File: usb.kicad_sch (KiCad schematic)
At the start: 0 parts

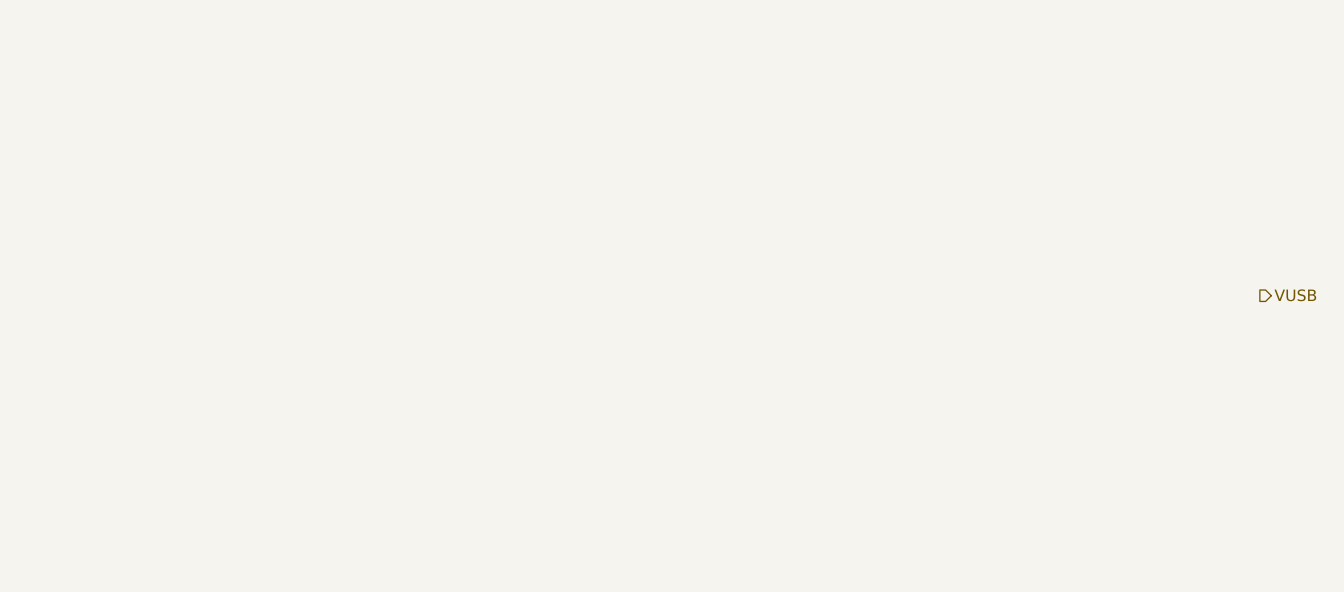
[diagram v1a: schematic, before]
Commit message: Finish rough layout
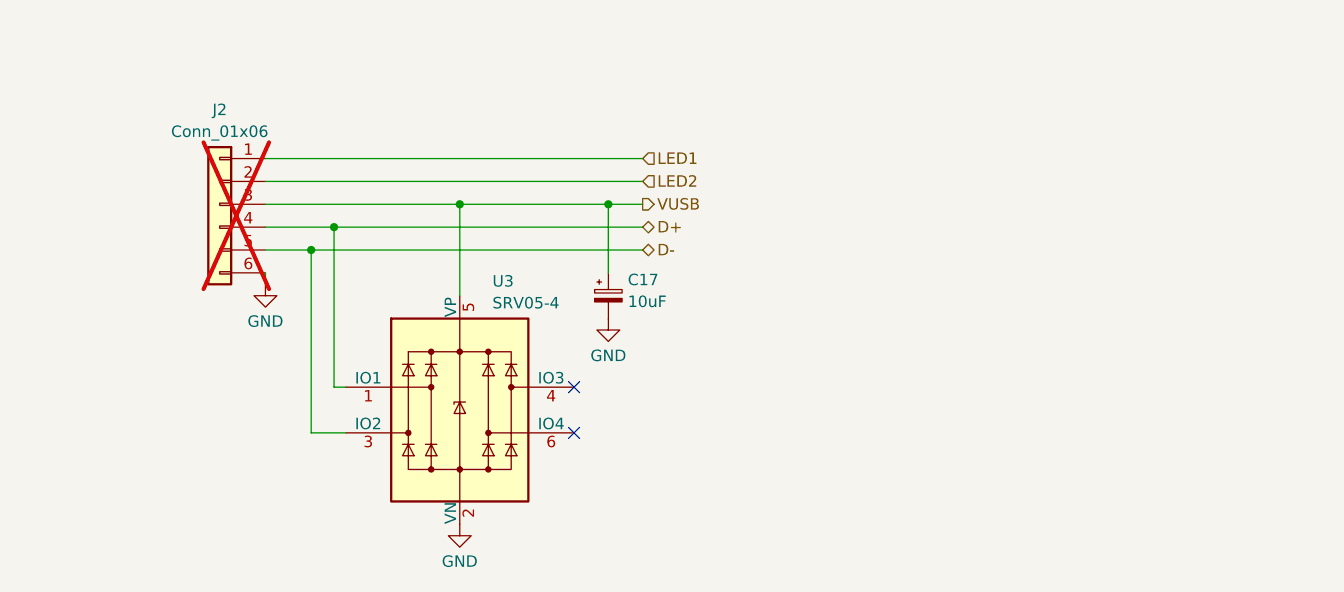
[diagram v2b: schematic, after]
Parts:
- added C17: 10uF, Capacitor_Tantalum_SMD:CP_EIA-3216-18_Kemet-A, symbol Device:C_Polarized_Small
- added J2: Conn_01x06, Connector_PinHeader_2.00mm:PinHeader_1x06_P2.00mm_Vertical, symbol Connector_Generic:Conn_01x06
- added U3: SRV05-4, Package_TO_SOT_SMD:SOT-23-6, symbol Power_Protection:SRV05-4
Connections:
- net VUSB: now also C17.1, J2.3 (Pin_3), U3.5 (VP)
- new net D+: J2.4 (Pin_4), U3.1 (IO1)
- new net D-: J2.5 (Pin_5), U3.3 (IO2)
- new net GND: C17.2, J2.6 (Pin_6), U3.2 (VN)
- new net LED1: J2.1 (Pin_1)
- new net LED2: J2.2 (Pin_2)
- no-connect marks 0 -> 2
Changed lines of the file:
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@@
 (kicad_sch (version 20230121) (generator eeschema)
   (paper "A4")
-  (hierarchical_label "VUSB" (shape output) (at 233.68 82.55 0) (fields_autoplaced)
-    (effects (font (size 1.27 1.27)) (justify left))
+  (junction (at 144.78 72.39) (diameter 0) (color 0 0 0 0)
+  )
+  (junction (at 130.81 74.93) (diameter 0) (color 0 0 0 0)
+  )
+  (junction (at 128.27 77.47) (diameter 0) (color 0 0 0 0)
+  )
+  (junction (at 161.29 72.39) (diameter 0) (color 0 0 0 0)
+  )
+  (no_connect (at 157.48 92.71))
+  (no_connect (at 157.48 97.79))
+  (wire (pts (xy 123.19 72.39) (xy 144.78 72.39))
+    (stroke (width 0) (type default))
+  )
+  (wire (pts (xy 123.19 80.01) (xy 123.19 81.28))
+    (stroke (width 0) (type default))
+  )
+  (wire (pts (xy 132.08 92.71) (xy 130.81 92.71))
+    (stroke (width 0) (type default))
+  )
+  (wire (pts (xy 130.81 74.93) (xy 165.1 74.93))
+    (stroke (width 0) (type default))
+  )
+  (wire (pts (xy 144.78 72.39) (xy 144.78 82.55))
+    (stroke (width 0) (type default))
+  )
+  (wire (pts (xy 128.27 97.79) (xy 128.27 77.47))
+    (stroke (width 0) (type default))
+  )
+  (wire (pts (xy 165.1 72.39) (xy 161.29 72.39))
+    (stroke (width 0) (type default))
+  )
+  (wire (pts (xy 123.19 74.93) (xy 130.81 74.93))
+    (stroke (width 0) (type default))
+  )
+  (wire (pts (xy 123.19 67.31) (xy 165.1 67.31))
+    (stroke (width 0) (type default))
+  )
+  (wire (pts (xy 161.29 72.39) (xy 161.29 80.01))
+    (stroke (width 0) (type default))
+  )
+  (wire (pts (xy 144.78 72.39) (xy 161.29 72.39))
+    (stroke (width 0) (type default))
+  )
+  (wire (pts (xy 123.19 77.47) (xy 128.27 77.47))
+    (stroke (width 0) (type default))
+  )
+  (wire (pts (xy 130.81 74.93) (xy 130.81 92.71))
+    (stroke (width 0) (type default))
+  )
+  (wire (pts (xy 123.19 69.85) (xy 165.1 69.85))
+    (stroke (width 0) (type default))
+  )
+  (wire (pts (xy 128.27 77.47) (xy 165.1 77.47))
+    (stroke (width 0) (type default))
+  )
+  (wire (pts (xy 132.08 97.79) (xy 128.27 97.79))
+    (stroke (width 0) (type default))
+  )
+  (hierarchical_label "LED1" (shape input) (at 165.1 67.31 0) (fields_autoplaced)
+    (effects (font (size 1.27 1.27)) (justify left))
+  )
+  (hierarchical_label "LED2" (shape input) (at 165.1 69.85 0) (fields_autoplaced)
+    (effects (font (size 1.27 1.27)) (justify left))
+  )
+  (hierarchical_label "D-" (shape bidirectional) (at 165.1 77.47 0) (fields_autoplaced)
+    (effects (font (size 1.27 1.27)) (justify left))
+  )
+  (hierarchical_label "D+" (shape bidirectional) (at 165.1 74.93 0) (fields_autoplaced)
+    (effects (font (size 1.27 1.27)) (justify left))
+  )
+  (hierarchical_label "VUSB" (shape output) (at 165.1 72.39 0) (fields_autoplaced)
+    (effects (font (size 1.27 1.27)) (justify left))
+  )
+  (symbol (lib_id "power:GND") (at 161.29 85.09 0) (unit 1)
+    (in_bom yes) (on_board yes) (dnp no) (fields_autoplaced)
+    (property "Reference" "#PWR036" (at 161.29 91.44 0)
+      (effects (font (size 1.27 1.27)) hide)
+    )
+    (property "Value" "GND" (at 161.29 89.2231 0)
+      (effects (font (size 1.27 1.27)))
+    )
+    (property "Footprint" "" (at 161.29 85.09 0)
+      (effects (font (size 1.27 1.27)) hide)
+    )
+    (property "Datasheet" "" (at 161.29 85.09 0)
+      (effects (font (size 1.27 1.27)) hide)
+    )
+    (pin "1")
+    (instances
+      (project "blinkekatze"
+        (path "/20b2a5b0-0a80-4b97-84d4-d5290b2926e5/8601bd41-9983-455b-8dd5-e9b320509b2a"
+          (reference "#PWR036") (unit 1)
+        )
+      )
+    )
+  )
+  (symbol (lib_id "Device:C_Polarized_Small") (at 161.29 82.55 0) (unit 1)
+    (in_bom yes) (on_board yes) (dnp no) (fields_autoplaced)
+    (property "Reference" "C17" (at 163.449 80.7918 0)
+      (effects (font (size 1.27 1.27)) (justify left))
+    )
+    (property "Value" "10uF" (at 163.449 83.216 0)
+      (effects (font (size 1.27 1.27)) (justify left))
+    )
+    (property "Footprint" "Capacitor_Tantalum_SMD:CP_EIA-3216-18_Kemet-A" (at 161.29 82.55 0)
+      (effects (font (size 1.27 1.27)) hide)
+    )
+    (property "Datasheet" "~" (at 161.29 82.55 0)
+      (effects (font (size 1.27 1.27)) hide)
+    )
+    (property "LCSC" "C7171" (at 161.29 82.55 0)
+      (effects (font (size 1.27 1.27)) hide)
+    )
+    (pin "1")
+    (pin "2")
+    (instances
+      (project "blinkekatze"
+        (path "/20b2a5b0-0a80-4b97-84d4-d5290b2926e5/8601bd41-9983-455b-8dd5-e9b320509b2a"
+          (reference "C17") (unit 1)
+        )
+      )
+    )
+  )
+  (symbol (lib_id "power:GND") (at 123.19 81.28 0) (unit 1)
+    (in_bom yes) (on_board yes) (dnp no) (fields_autoplaced)
+    (property "Reference" "#PWR035" (at 123.19 87.63 0)
+      (effects (font (size 1.27 1.27)) hide)
+    )
+    (property "Value" "GND" (at 123.19 85.4131 0)
+      (effects (font (size 1.27 1.27)))
+    )
+    (property "Footprint" "" (at 123.19 81.28 0)
+      (effects (font (size 1.27 1.27)) hide)
+    )
+    (property "Datasheet" "" (at 123.19 81.28 0)
+      (effects (font (size 1.27 1.27)) hide)
+    )
+    (pin "1")
+    (instances
+      (project "blinkekatze"
+        (path "/20b2a5b0-0a80-4b97-84d4-d5290b2926e5/8601bd41-9983-455b-8dd5-e9b320509b2a"
+          (reference "#PWR035") (unit 1)
+        )
+      )
+    )
+  )
+  (symbol (lib_id "Power_Protection:SRV05-4") (at 144.78 95.25 0) (unit 1)
+    (in_bom yes) (on_board yes) (dnp no) (fields_autoplaced)
+    (property "Reference" "U3" (at 148.4061 80.9457 0)
+      (effects (font (size 1.27 1.27)) (justify left))
+    )
+    (property "Value" "SRV05-4" (at 148.4061 83.3699 0)
+      (effects (font (size 1.27 1.27)) (justify left))
+    )
+    (property "Footprint" "Package_TO_SOT_SMD:SOT-23-6" (at 162.56 106.68 0)
+      (effects (font (size 1.27 1.27)) hide)
+    )
+    (property "Datasheet" "http://www.onsemi.com/pub/Collateral/SRV05-4-D.PDF" (at 144.78 95.25 0)
+      (effects (font (size 1.27 1.27)) hide)
+    )
+    (property "LCSC" "C85364" (at 144.78 95.25 0)
+      (effects (font (size 1.27 1.27)) hide)
+    )
+    (pin "1")
+    (pin "2")
+    (pin "3")
+    (pin "4")
+    (pin "5")
+    (pin "6")
+    (instances
+      (project "blinkekatze"
+        (path "/20b2a5b0-0a80-4b97-84d4-d5290b2926e5/8601bd41-9983-455b-8dd5-e9b320509b2a"
+          (reference "U3") (unit 1)
+        )
+      )
+    )
+  )
+  (symbol (lib_id "power:GND") (at 144.78 107.95 0) (unit 1)
+    (in_bom yes) (on_board yes) (dnp no) (fields_autoplaced)
+    (property "Reference" "#PWR037" (at 144.78 114.3 0)
+      (effects (font (size 1.27 1.27)) hide)
+    )
+    (property "Value" "GND" (at 144.78 112.0831 0)
+      (effects (font (size 1.27 1.27)))
+    )
+    (property "Footprint" "" (at 144.78 107.95 0)
+      (effects (font (size 1.27 1.27)) hide)
+    )
+    (property "Datasheet" "" (at 144.78 107.95 0)
+      (effects (font (size 1.27 1.27)) hide)
+    )
+    (pin "1")
+    (instances
+      (project "blinkekatze"
+        (path "/20b2a5b0-0a80-4b97-84d4-d5290b2926e5/8601bd41-9983-455b-8dd5-e9b320509b2a"
+          (reference "#PWR037") (unit 1)
+        )
+      )
+    )
+  )
+  (symbol (lib_id "Connector_Generic:Conn_01x06") (at 118.11 72.39 0) (mirror y) (unit 1)
+    (in_bom no) (on_board yes) (dnp yes) (fields_autoplaced)
+    (property "Reference" "J2" (at 118.11 61.8957 0)
+      (effects (font (size 1.27 1.27)))
+    )
+    (property "Value" "Conn_01x06" (at 118.11 64.3199 0)
+      (effects (font (size 1.27 1.27)))
+    )
+    (property "Footprint" "Connector_PinHeader_2.00mm:PinHeader_1x06_P2.00mm_Vertical" (at 118.11 72.39 0)
+      (effects (font (size 1.27 1.27)) hide)
+    )
+    (property "Datasheet" "~" (at 118.11 72.39 0)
+      (effects (font (size 1.27 1.27)) hide)
+    )
+    (pin "1")
+    (pin "2")
+    (pin "3")
+    (pin "4")
+    (pin "5")
+    (pin "6")
+    (instances
+      (project "blinkekatze"
+        (path "/20b2a5b0-0a80-4b97-84d4-d5290b2926e5/8601bd41-9983-455b-8dd5-e9b320509b2a"
+          (reference "J2") (unit 1)
+        )
+      )
+    )
   )
 )

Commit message: Relayout board to fit constraints of Micro USB Blinkekatzen
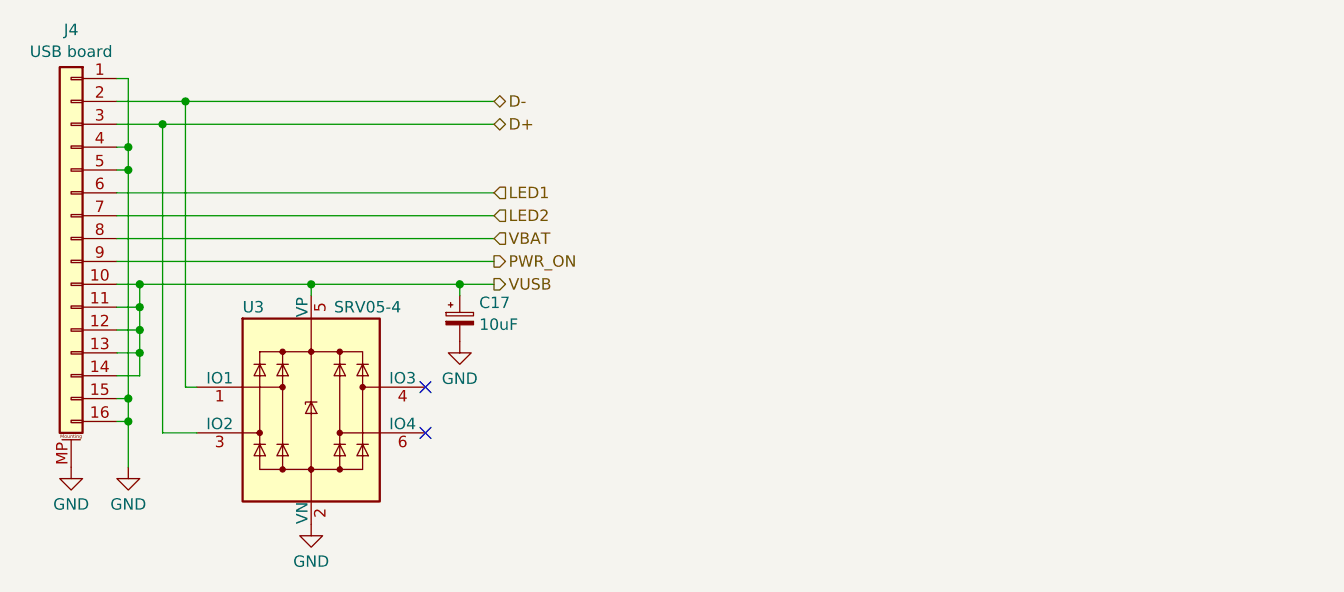
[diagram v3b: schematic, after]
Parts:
- removed J2: Conn_01x06, Connector_PinHeader_2.00mm:PinHeader_1x06_P2.00mm_Vertical, symbol Connector_Generic:Conn_01x06
- added J4: USB board, Connector_FFC-FPC_HDGC:0.5K-QX-16PWB_16Pin_0.5mm, symbol Connector_Generic_MountingPin:Conn_01x16_MountingPin
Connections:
- net D+: now also U3.3 (IO2), J4.3 (Pin_3); no longer U3.1 (IO1)
- net D-: now also U3.1 (IO1), J4.2 (Pin_2); no longer U3.3 (IO2)
- net GND: now also J4.1 (Pin_1), J4.15 (Pin_15), J4.16 (Pin_16), J4.4 (Pin_4), J4.5 (Pin_5), J4.MP (MountPin)
- net LED1: now also J4.6 (Pin_6)
- net LED2: now also J4.7 (Pin_7)
- net VUSB: now also J4.10 (Pin_10), J4.11 (Pin_11), J4.12 (Pin_12), J4.13 (Pin_13), J4.14 (Pin_14)
- new net PWR_ON: J4.9 (Pin_9)
- new net VBAT: J4.8 (Pin_8)
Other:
- moved on the sheet: C17, U3
